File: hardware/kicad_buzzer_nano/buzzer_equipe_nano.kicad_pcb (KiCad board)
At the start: 2 copper layers, 120 x 140 mm, 8 parts, among them J1 nRF24L01+ (headers femelles) 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, J2 Module charge TP4056+protect+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, J3 Module vibreur IN/VCC/GND, SW1 Bouton BUZZ (fils volants), SW2 Interrupteur marche/arret (fi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

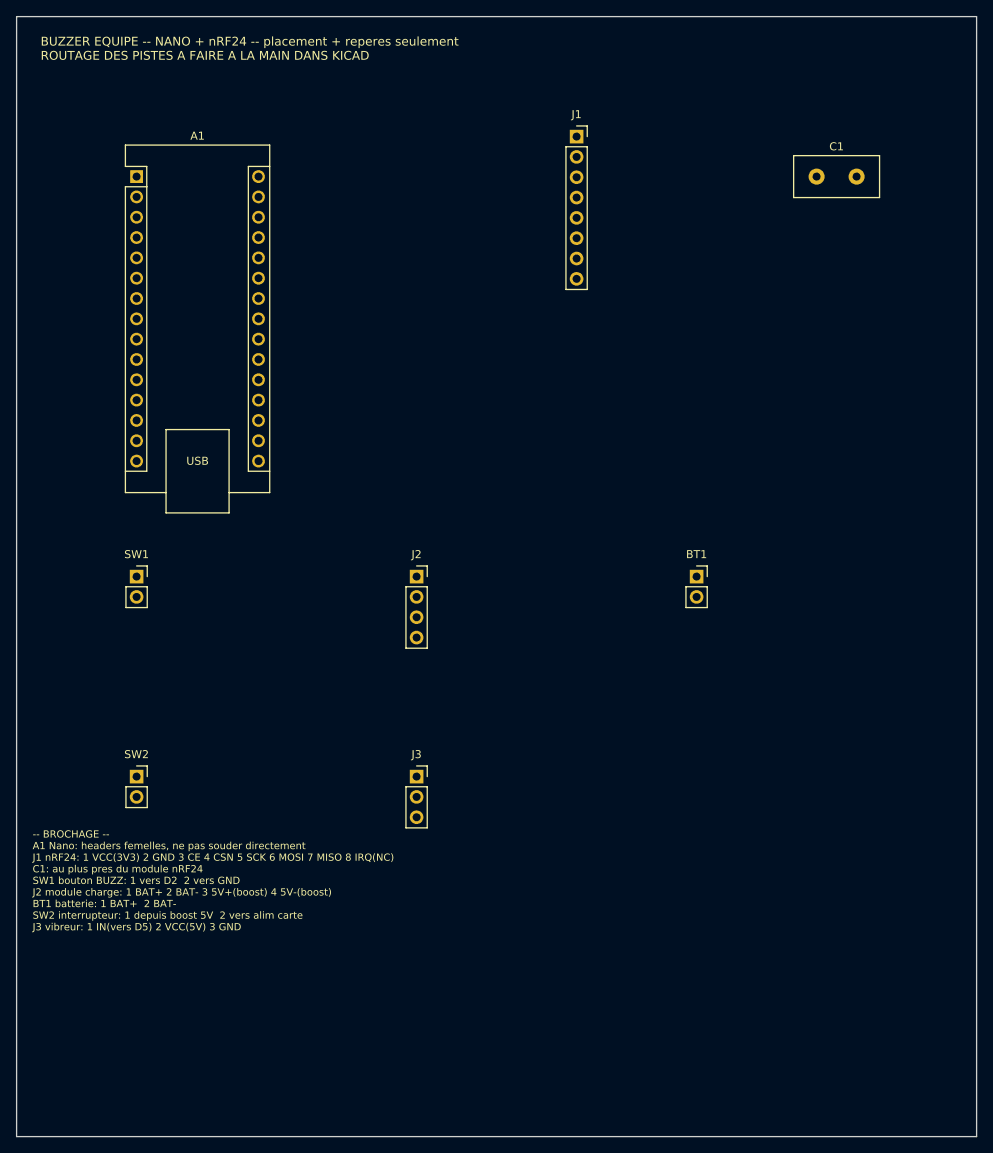
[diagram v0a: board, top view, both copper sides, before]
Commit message: hardware: pistes routees sur les 3 cartes (Freerouting + kicad-cli pcb drc)
Autoroutage headless via Freerouting (pcbnew.ExportSpecctraDSN -> java -jar
freerouting.jar -> pcbnew.ImportSpecctraSES), pas un routage devine a la
main. Resultat verifie avec kicad-cli pcb drc reel sur les 3 cartes: 0
violation de clearance, 0 element non connecte. Seuls avertissements
restants: lib_footprint_mismatch (cosmetique) et quelques track_dangling
(residu mineur d'autorouter, a nettoyer dans KiCad, sans impact electrique).

Co-Authored-By: Claude Sonnet 5 <noreply@anthropic.com>
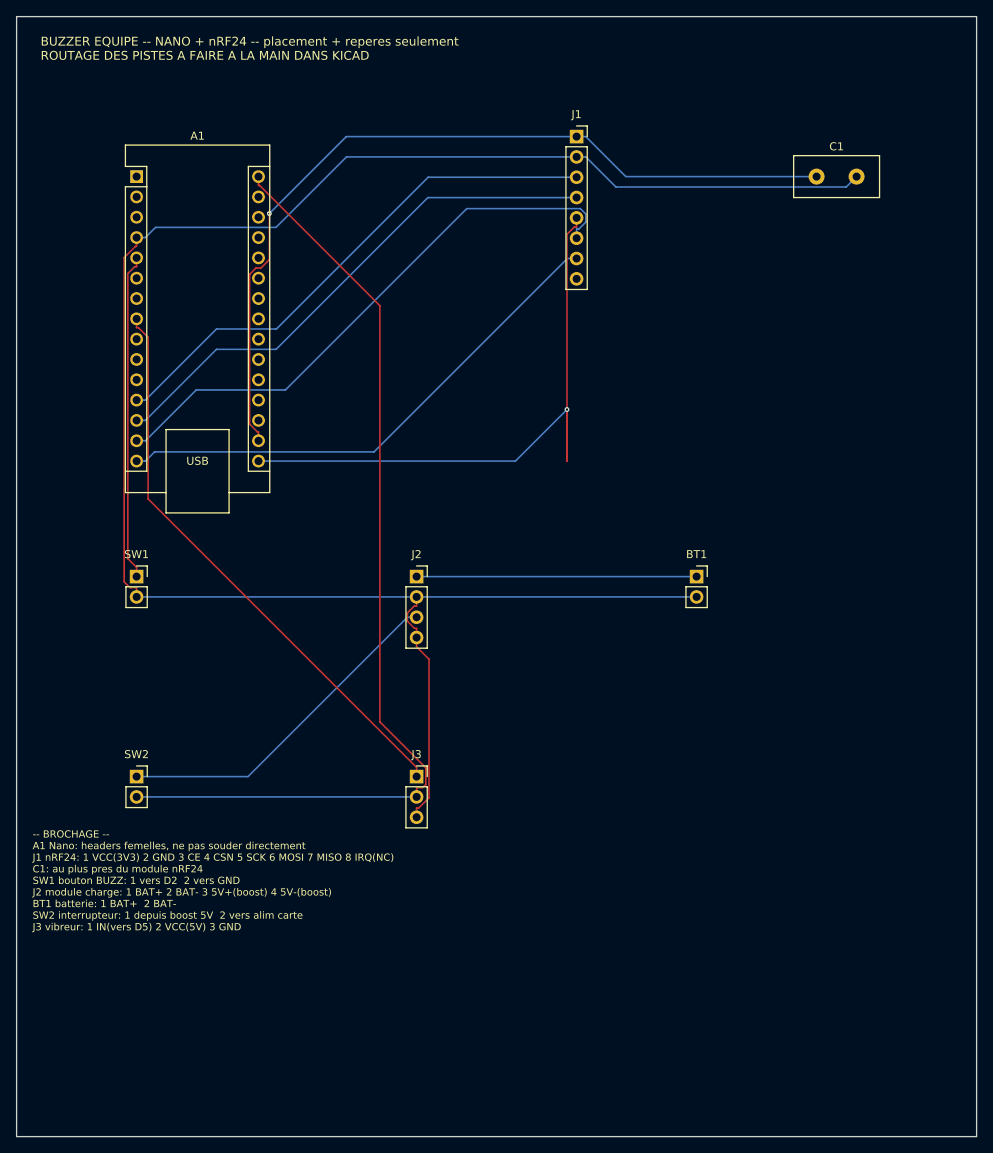
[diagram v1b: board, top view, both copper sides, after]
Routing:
- net GND: track 0.00 -> 243.3 mm
- net VCC_5V_SW: track 0.00 -> 122.2 mm
- net +3V3: track 0.00 -> 104.8 mm, vias 0 -> 1
- net NRF_SCK: track 0.00 -> 91.6 mm, vias 0 -> 1
- net NRF_MOSI: track 0.00 -> 72.1 mm
- net VIBE_IN: track 0.00 -> 71.9 mm
- net NRF_CSN: track 0.00 -> 66.5 mm
- net NRF_CE: track 0.00 -> 66.5 mm
- net NRF_MISO: track 0.00 -> 65.5 mm
- net VCC_5V_RAW: track 0.00 -> 43.3 mm
- net BTN_SIG: track 0.00 -> 40.9 mm
- net BAT_PLUS: track 0.00 -> 35.0 mm

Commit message: hardware: nettoyage track_dangling + C3 rapproche de J_NRF sur le hub
Nano: 2 troncons de piste dupliques/morts (net NRF_SCK) identifies et
supprimes via script pcbnew, ne menaient a aucune pastille -- DRC propre
(0 track_dangling, 0 non connecte, seul lib_footprint_mismatch cosmetique
reste).

Hub: le nRF24 (J_NRF) et son condensateur de decouplage dedie (C3) etaient
a 25mm -- trop loin pour un decouplage propre a 2,4GHz. C3 repositionne a
12mm de J_NRF, carte entierement re-routee (Freerouting), puis 2 nouveaux
track_dangling (net VCC_5V_MEGA) nettoyes de la meme facon. DRC final: 0
violation de clearance, 0 non connecte, 0 track_dangling.

Co-Authored-By: Claude Sonnet 5 <noreply@anthropic.com>
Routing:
- net NRF_SCK: track 91.6 -> 65.9 mm
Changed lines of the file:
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@@
-	)
-	(segment
-		(start 73.7973 60.56)
-		(end 73.7973 54.1185)
-		(width 0.2)
-		(layer "F.Cu")
-		(net 10)
-	)
-	(segment
-		(start 73.7973 54.1185)
-		(end 73.7973 60.56)
-		(width 0.2)
-		(layer "F.Cu")
-		(net 10)
 	)
 	(segment
@@
 	)
 	(segment
-		(start 73.7973 60.56)
-		(end 73.7973 54.1185)
-		(width 0.2)
-		(layer "B.Cu")
-		(net 10)
-	)
-	(segment
 		(start 73.7973 54.1185)
 		(end 67.3558 60.56)
 		(width 0.2)
 		(layer "B.Cu")
-		(net 10)
-	)
-	(segment
-		(start 73.7973 54.1185)
-		(end 73.7973 60.56)
-		(width 0.2)
-		(layer "B.Cu")

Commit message: hardware: vrais ports femelles pour les modules (Nano, ESP32 x2) + reroutage
Remplace les empreintes abstraites/simplifiees par de vraies barrettes
femelles PinSocket, dimensionnees et brochees pour correspondre aux modules
physiques reels, sur les 3 cartes:

- Nano (buzzer equipe): 2x PinSocket_1x15 (A1L/A1R, 30 broches, entraxe
  15,24mm) au lieu de l'empreinte "Nano soude directement" -- numerotation
  verifiee contre la vraie empreinte Module:Arduino_Nano.
- ESP32 buzzer (secours): 2x PinSocket_1x19 (U1L/U1R, 38 broches, entraxe
  22,86mm) au lieu du connecteur 4 broches abstrait -- brochage GPIO4/
  GPIO13/VIN/GND positionne selon le layout generique 38 broches le plus
  courant (verifie en ligne), avec avertissement clair dans le README:
  plusieurs variantes de clones existent, a verifier sur le module recu.
- ESP32 hub (regie): 2x PinSocket_1x15 (U_ESP32L/R, 30 broches, entraxe
  15,24mm) au lieu du connecteur 12 broches abstrait -- brochage DOIT ESP32
  DevKit V1 verifie (le modele exact confirme par le client), design de
  reference unique donc plus fiable que les clones 38 broches.

Les 34/19 broches physiques non utilisees sur chaque module restent
presentes sans net (fixation mecanique uniquement). Toutes les cartes
re-routees (Freerouting) et revalidees (kicad-cli pcb drc): 0 violation de
clearance, 0 element non connecte, 0 track_dangling restant (nettoyage
verifie topologie par topologie pour ne pas casser une piste utile).

Co-Authored-By: Claude Sonnet 5 <noreply@anthropic.com>
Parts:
- removed A1: Arduino Nano (sur headers femelles, pas soude), Module:Arduino_Nano
- added A1L: Nano colonne gauche (broches 1-15), Connector_PinSocket_2.54mm:PinSocket_1x15_P2.54mm_Vertical, F.Cu at (20.0, 25.0)
- added A1R: Nano colonne droite (broches 16-30), Connector_PinSocket_2.54mm:PinSocket_1x15_P2.54mm_Vertical, F.Cu at (35.2, 25.0)
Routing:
- net NRF_SCK: track 65.9 -> 55.9 mm, vias 1 -> 0
- net VIBE_IN: track 71.9 -> 79.1 mm, vias 0 -> 1
- net NRF_MOSI: track 72.1 -> 65.5 mm
- net VCC_5V_SW: track 122.2 -> 116.2 mm, vias 0 -> 1
- net +3V3: track 104.8 -> 109.8 mm
- net NRF_MISO: track 65.5 -> 66.5 mm
- net GND: track 243.3 -> 244.2 mm
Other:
- board text added: "-- BROCHAGE -- A1L/A1R: 2 barrettes femelles 1x15 (colonne gauche 1-15 / droite 16-30) -- le Nano s'enfiche dessus, pas de soudure directe J1 nRF24: 1 VCC(3V3) 2 GND 3 CE 4 CSN 5 SCK 6 MOSI 7 MISO 8 IRQ(NC) C1: au plus pres du module nRF24 SW1 bouton BUZZ: 1 vers D2 2 vers GND J2 module charge: 1 BAT+ 2 BAT- 3 5V+(boost) 4 5V-(boost) BT1 batterie: 1 BAT+ 2 BAT- SW2 interrupteur: 1 depuis boost 5V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"
- board text removed: "-- BROCHAGE -- A1 Nano: headers femelles, ne pas souder directement J1 nRF24: 1 VCC(3V3) 2 GND 3 CE 4 CSN 5 SCK 6 MOSI 7 MISO 8 IRQ(NC) C1: au plus pres du module nRF24 SW1 bouton BUZZ: 1 vers D2 2 vers GND J2 module charge: 1 BAT+ 2 BAT- 3 5V+(boost) 4 5V-(boost) BT1 batterie: 1 BAT+ 2 BAT- SW2 interrupteur: 1 depuis boost 5V 2 vers alim carte J3 vibreur: 1 IN(vers D5) 2 VCC(5V) 3 GND"

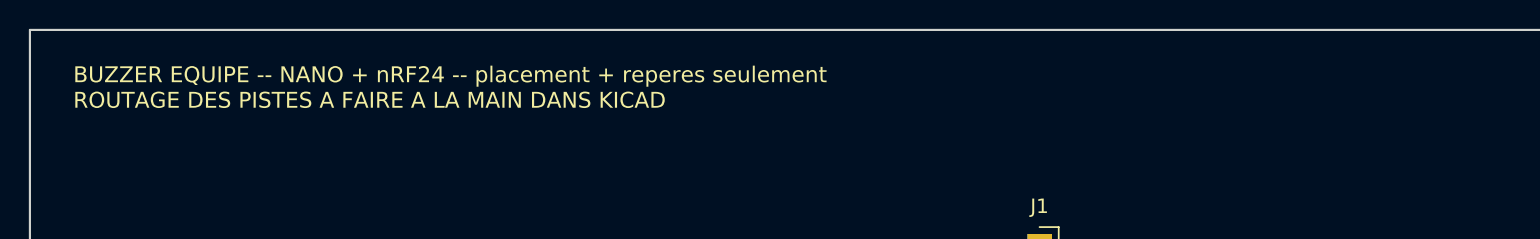
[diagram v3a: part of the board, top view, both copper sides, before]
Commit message: hardware: retire la mention "routage a faire a la main" (obsolete)
Le texte de titre sur la serigraphie des 3 cartes disait encore "ROUTAGE
DES PISTES A FAIRE A LA MAIN DANS KICAD", ecrit avant que le routage ne
soit fait via Freerouting. Remplace par une mention correcte ("pistes
routees (Freerouting), a relire avant fabrication"). Edition de texte
seule sur les fichiers deja routes -- aucune piste/pastille touchee,
DRC revalide identique (0 violation de clearance, 0 non connecte).

Co-Authored-By: Claude Sonnet 5 <noreply@anthropic.com>
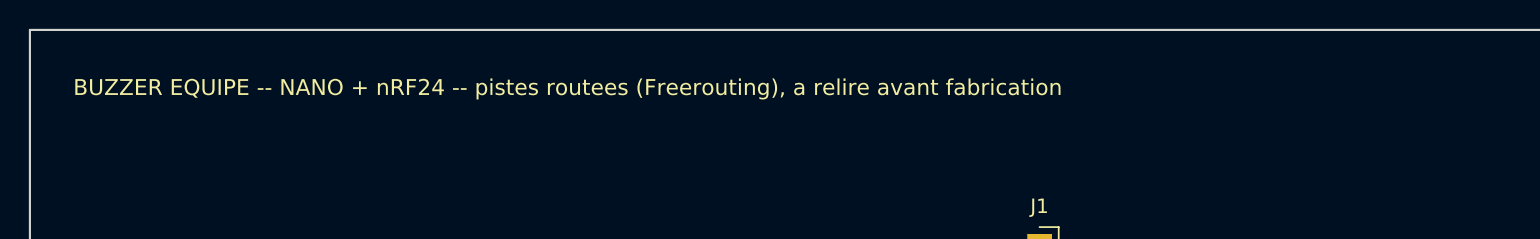
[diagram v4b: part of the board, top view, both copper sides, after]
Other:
- board text added: "BUZZER EQUIPE -- NANO + nRF24 -- pistes routees (Freerouting), a relire avant fabrication"
- board text removed: "BUZZER EQUIPE -- NANO + nRF24 -- placement + reperes seulement ROUTAGE DES PISTES A FAIRE A LA MAIN DANS KICAD"
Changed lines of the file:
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@@
 		)
 	)
-	(gr_text "BUZZER EQUIPE -- NANO + nRF24 -- placement + reperes seulement\nROUTAGE DES PISTES A FAIRE A LA MAIN DANS KICAD"
+	(gr_text "BUZZER EQUIPE -- NANO + nRF24 -- pistes routees (Freerouting), a relire avant fabrication"
 		(at 8 9 0)
 		(layer "F.SilkS")

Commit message: hardware: titres serigraphie simplifies (retire tout commentaire de process)
Le titre en haut de chaque carte disait encore des phrases du type "pistes
routees (Freerouting), a relire avant fabrication" -- du commentaire sur le
processus de generation, pas quelque chose qui a sa place gravee sur un vrai
circuit fabrique. Remplace par un simple nom de carte ("BUZZER EQUIPE -
NANO", "BUZZER EQUIPE - ESP32", "REGIE HUB"). Le bloc BROCHAGE (guide de
soudage demande explicitement) reste inchange. Edition de texte seule,
DRC revalide identique sur les 3 cartes.

Co-Authored-By: Claude Sonnet 5 <noreply@anthropic.com>
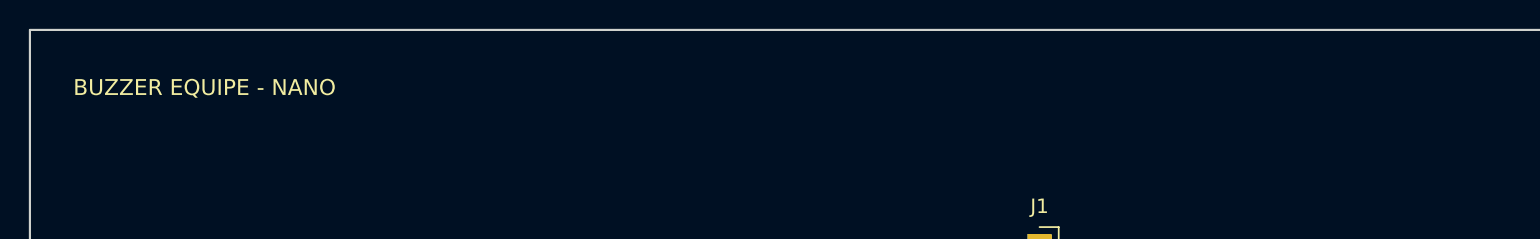
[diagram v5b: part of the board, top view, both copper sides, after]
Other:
- board text added: "BUZZER EQUIPE - NANO"
- board text removed: "BUZZER EQUIPE -- NANO + nRF24 -- pistes routees (Freerouting), a relire avant fabrication"
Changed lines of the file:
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@@
 		)
 	)
-	(gr_text "BUZZER EQUIPE -- NANO + nRF24 -- pistes routees (Freerouting), a relire avant fabrication"
+	(gr_text "BUZZER EQUIPE - NANO"
 		(at 8 9 0)
 		(layer "F.SilkS")

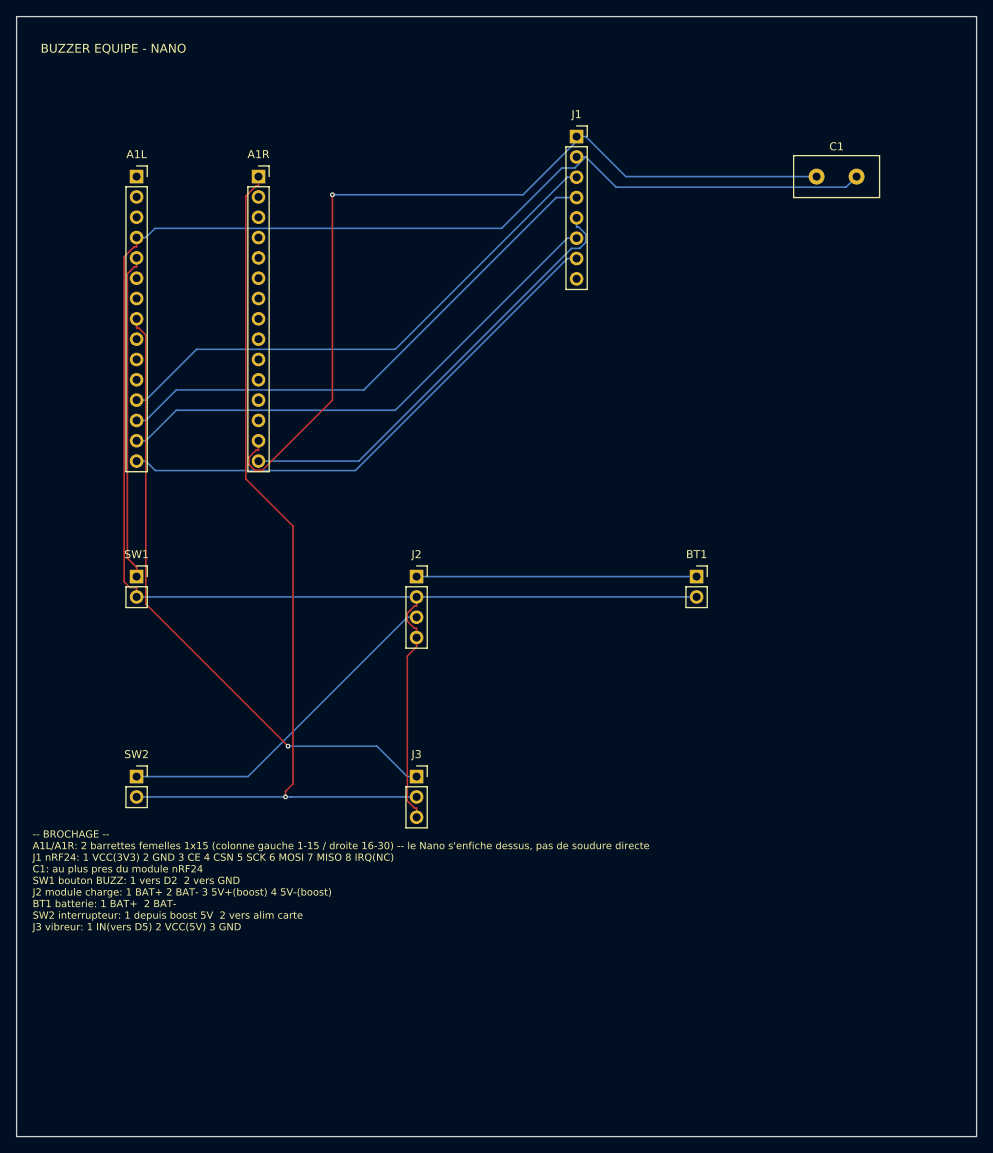
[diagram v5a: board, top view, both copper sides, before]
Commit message: hardware: corrige VCC/GND nRF24 (inverses) + passe en 2x4 (module PA+LNA)
En reponse a "le nrf24 c'est sur une ligne ?", verification du brochage
nRF24 contre 3 sources independantes (components101.com,
lastminuteengineers.com, doc generale nRF24L01+) : la broche 1 est GND et
la broche 2 est VCC, pas l'inverse comme c'etait cable jusqu'ici sur J1
(carte Nano) et J_NRF (carte hub) -- schema ET PCB. Broche 1 = toujours la
pastille carree sur cette empreinte, coherent avec "GND identifiable par
son marquage carre" documente pour ce module.

Le module confirme etant un nRF24L01+PA+LNA (longue portee), son connecteur
est 2x4 et non 1x8 standard -- empreinte changee vers PinSocket_2x04 sur
les 2 cartes concernees, brochage 1=GND 2=VCC puis CE/CSN/SCK/MOSI/MISO/IRQ
sur les rangees suivantes (ordre le plus courant publie, mais AUCUN
standard universel n'existe pour les variantes PA+LNA -- avertissement
explicite dans le README et sur la serigraphie: verifier sur le module
recu avant de souder).

Schemas re-verifies (kicad-cli sch erc, memes comptes qu'avant -- aucune
regression). PCB re-routes (Freerouting) et revalides (kicad-cli pcb drc):
0 violation de clearance, 0 element non connecte, 0 track_dangling.

Co-Authored-By: Claude Sonnet 5 <noreply@anthropic.com>
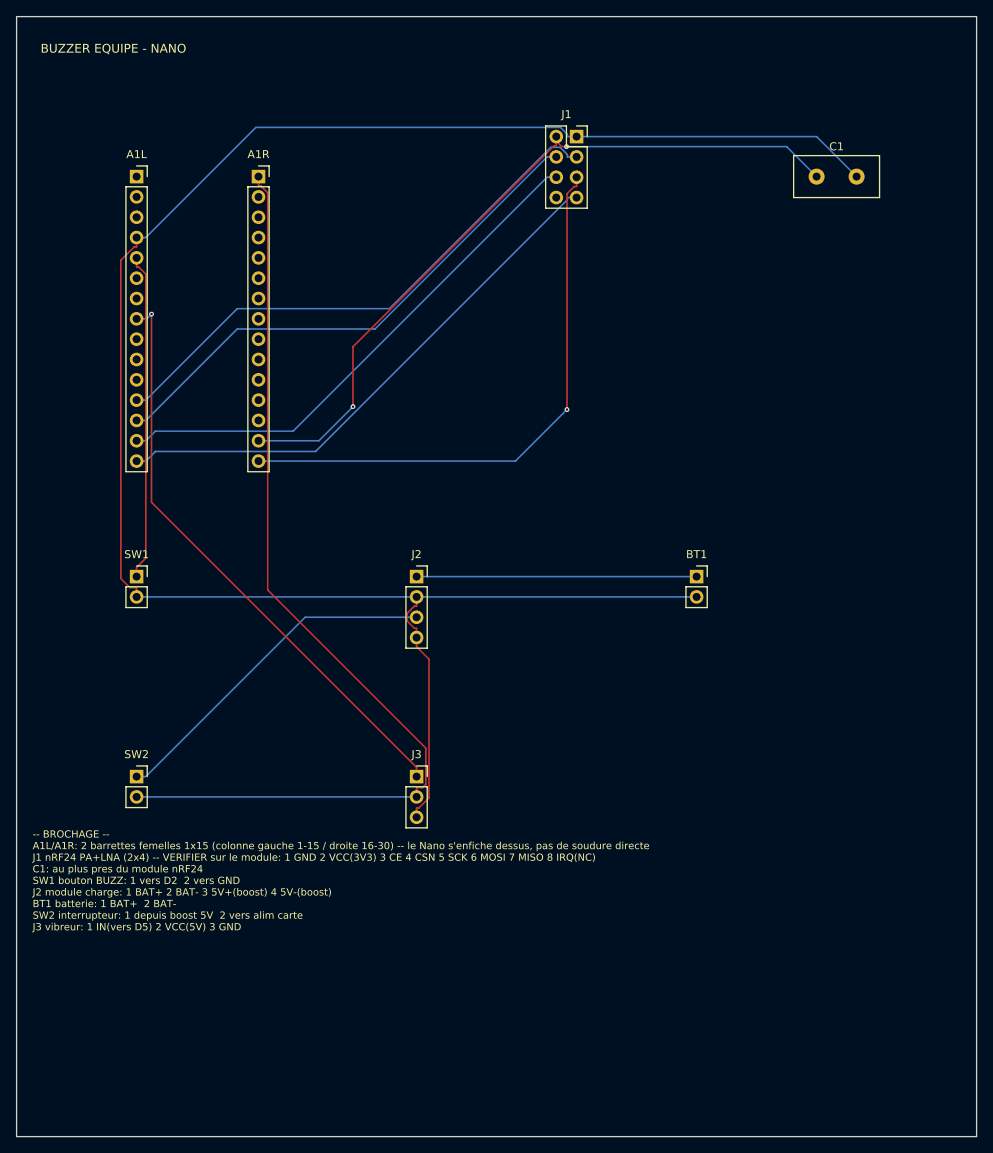
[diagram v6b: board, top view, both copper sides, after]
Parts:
- J1: value nRF24L01+ (headers femelles) - VCC=3V3 UNIQUEMENT -> nRF24L01+PA+LNA - VERIFIER le brochage sur le module recu; footprint Connector_PinSocket_2.54mm:PinSocket_1x08_P2.54mm_Vertical -> Connector_PinSocket_2.54mm:PinSocket_2x04_P2.54mm_Vertical
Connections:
- J1 pad 1: +3V3 -> GND
- J1 pad 2: GND -> +3V3
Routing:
- net +3V3: track 109.8 -> 92.5 mm, vias 1 -> 2
- net NRF_SCK: track 55.9 -> 70.9 mm, vias 0 -> 1
- net VCC_5V_SW: track 116.2 -> 122.3 mm, vias 1 -> 0
- net VIBE_IN: track 79.1 -> 73.7 mm
- net NRF_MISO: track 66.5 -> 68.8 mm
- net NRF_CE: track 66.5 -> 68.8 mm
- net GND: track 244.2 -> 245.9 mm
- net NRF_MOSI: track 65.5 -> 66.1 mm
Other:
- board text added: "-- BROCHAGE -- A1L/A1R: 2 barrettes femelles 1x15 (colonne gauche 1-15 / droite 16-30) -- le Nano s'enfiche dessus, pas de soudure directe J1 nRF24 PA+LNA (2x4) -- VERIFIER sur le module: 1 GND 2 VCC(3V3) 3 CE 4 CSN 5 SCK 6 MOSI 7 MISO 8 IRQ(NC) C1: au plus pres du module nRF24 SW1 bouton BUZZ: 1 vers D2 2 vers GND J2 module charge: 1 BAT+ 2 BAT- 3 5V+(boost) 4 5V-(boost) BT1 batterie: 1 BAT+ 2 B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"
- board text removed: "-- BROCHAGE -- A1L/A1R: 2 barrettes femelles 1x15 (colonne gauche 1-15 / droite 16-30) -- le Nano s'enfiche dessus, pas de soudure directe J1 nRF24: 1 VCC(3V3) 2 GND 3 CE 4 CSN 5 SCK 6 MOSI 7 MISO 8 IRQ(NC) C1: au plus pres du module nRF24 SW1 bouton BUZZ: 1 vers D2 2 vers GND J2 module charge: 1 BAT+ 2 BAT- 3 5V+(boost) 4 5V-(boost) BT1 batterie: 1 BAT+ 2 BAT- SW2 interrupteur: 1 depuis boost 5V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"
